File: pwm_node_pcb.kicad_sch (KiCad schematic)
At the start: 49 parts, among them J1 Battery, J2 5V Breakout, J3 TC2050-IDC-NL, J4 CAN1, J5 Load Source, U1 LMR51430, U2 LD1117S33CTR, U3 TJA1051T/3, U4 STM32L432KCU, U5 TXB0104QPWRQ1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

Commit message: Fix silkscreen and load caps to 220uF
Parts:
- C16, C17: value 2200u -> 220u
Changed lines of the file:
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@@
 	(title_block
 		(title "PWM Node")
-		(rev "v0.1.0-alpha")
+		(rev "v0.1.0")
 		(company "Daniel Jeon")
 	)
@@
 			)
 		)
-		(property "Value" "2200u"
+		(property "Value" "220u"
 			(at 117.348 185.42 0)
 			(effects
@@
 			)
 		)
-		(property "Value" "2200u"
+		(property "Value" "220u"
 			(at 104.648 185.42 0)
 			(effects

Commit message: Fix flipped UART breakout (TP) nets
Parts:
- TP1: value UART_RX -> UART_TX
- TP2: value UART_TX -> UART_RX
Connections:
- net USART1_RX: now also TP2.1, U4.30 (PB7); no longer TP1.1, U4.29 (PB6)
- net USART1_TX: now also TP1.1, U4.29 (PB6); no longer TP2.1, U4.30 (PB7)
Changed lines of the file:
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@@
 		)
 	)
-	(hierarchical_label "USART1_TX"
+	(hierarchical_label "USART1_RX"
 		(shape input)
-		(at 157.48 156.21 180)
+		(at 57.15 134.62 180)
 		(effects
 			(font
@@
 		)
 	)
-	(hierarchical_label "USART1_RX"
+	(hierarchical_label "USART1_TX"
 		(shape input)
-		(at 157.48 148.59 180)
+		(at 57.15 132.08 180)
 		(effects
 			(font
@@
 		)
 	)
-	(hierarchical_label "CAN1_TX"
+	(hierarchical_label "USART1_TX"
 		(shape input)
-		(at 217.17 81.28 180)
+		(at 157.48 148.59 180)
 		(effects
 			(font
@@
 		)
 	)
-	(hierarchical_label "USART1_TX"
+	(hierarchical_label "CAN1_TX"
 		(shape input)
-		(at 57.15 134.62 180)
+		(at 217.17 81.28 180)
 		(effects
 			(font
@@
 		)
 	)
-	(hierarchical_label "USART1_RX"
+	(hierarchical_label "CAN1_RX"
 		(shape input)
-		(at 57.15 132.08 180)
+		(at 82.55 129.54 0)
 		(effects
 			(font
 				(size 1.27 1.27)
 			)
-			(justify right)
+			(justify left)
 		)
 	)
-	(hierarchical_label "CAN1_RX"
+	(hierarchical_label "TIM1_CH4"
 		(shape input)
-		(at 82.55 129.54 0)
+		(at 241.3 143.51 0)
 		(effects
 			(font
@@
 		)
 	)
-	(hierarchical_label "TIM1_CH4"
+	(hierarchical_label "USART1_RX"
 		(shape input)
-		(at 241.3 143.51 0)
+		(at 157.48 156.21 180)
 		(effects
 			(font
 				(size 1.27 1.27)
 			)
-			(justify left)
+			(justify right)
 		)
 	)
@@
 			)
 		)
-		(property "Value" "UART_TX"
+		(property "Value" "UART_RX"
 			(at 163.83 157.4799 90)
 			(effects
@@
 			)
 		)
-		(property "Value" "UART_RX"
+		(property "Value" "UART_TX"
 			(at 163.83 149.8599 90)
 			(effects

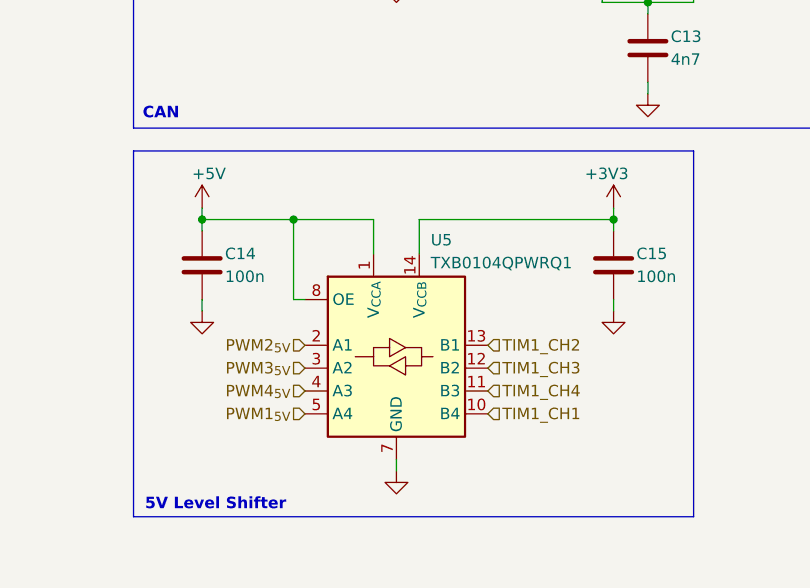
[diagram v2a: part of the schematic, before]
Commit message: Fix level shifter circuit
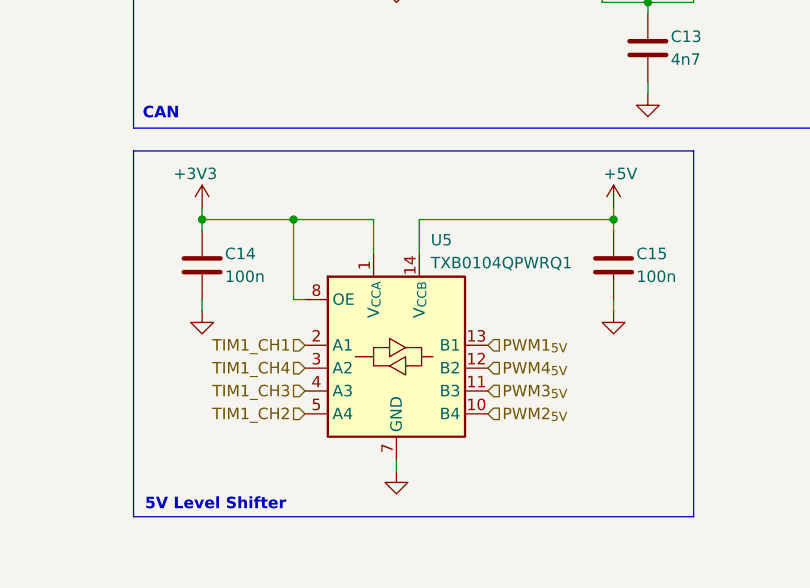
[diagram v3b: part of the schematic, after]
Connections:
- net +3V3: now also C14.1, U5.1 (V_{CCA}), U5.8 (OE); no longer C15.1, U5.14 (V_{CCB})
- net +5V: now also C15.1, U5.14 (V_{CCB}); no longer C14.1, U5.1 (V_{CCA}), U5.8 (OE)
- net PWM1_{5V}: now also U5.13 (B1); no longer U5.5 (A4)
- net PWM2_{5V}: now also U5.10 (B4); no longer U5.2 (A1)
- net PWM3_{5V}: now also U5.11 (B3); no longer U5.3 (A2)
- net PWM4_{5V}: now also U5.12 (B2); no longer U5.4 (A3)
- net TIM1_CH1: now also U5.2 (A1); no longer U5.10 (B4)
- net TIM1_CH2: now also U5.5 (A4); no longer U5.13 (B1)
- net TIM1_CH3: now also U5.4 (A3); no longer U5.12 (B2)
- net TIM1_CH4: now also U5.3 (A2); no longer U5.11 (B3)
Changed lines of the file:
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@@
 	)
 	(junction
+		(at 219.71 124.46)
+		(diameter 0)
+		(color 0 0 0 0)
+	)
+	(junction
 		(at 165.1 26.67)
 		(diameter 0)
@@
 	)
 	(junction
-		(at 219.71 124.46)
-		(diameter 0)
-		(color 0 0 0 0)
-	)
-	(junction
 		(at 209.55 124.46)
 		(diameter 0)
@@
 	(wire
 		(pts
+			(xy 219.71 124.46) (xy 228.6 124.46)
+		)
+		(stroke
+			(width 0)
+			(type default)
+		)
+	)
+	(wire
+		(pts
 			(xy 54.61 31.75) (xy 55.88 31.75)
 		)
@@
 	(wire
 		(pts
-			(xy 219.71 124.46) (xy 228.6 124.46)
-		)
-		(stroke
-			(width 0)
-			(type default)
-		)
-	)
-	(wire
-		(pts
 			(xy 76.2 80.01) (xy 76.2 81.28)
 		)
@@
 		)
 	)
-	(hierarchical_label "TIM1_CH1"
+	(hierarchical_label "PWM4_{5V}"
 		(shape input)
-		(at 241.3 146.05 0)
+		(at 241.3 140.97 0)
 		(effects
 			(font
@@
 	(hierarchical_label "PWM3_{5V}"
 		(shape input)
-		(at 220.98 140.97 180)
+		(at 241.3 143.51 0)
 		(effects
 			(font
 				(size 1.27 1.27)
 			)
-			(justify right)
+			(justify left)
 		)
 	)
@@
 		)
 	)
-	(hierarchical_label "TIM1_CH2"
+	(hierarchical_label "SWO"
 		(shape input)
-		(at 241.3 138.43 0)
+		(at 36.83 38.1 0)
 		(effects
 			(font
@@
 		)
 	)
-	(hierarchical_label "SWO"
+	(hierarchical_label "PWM2_{5V}"
 		(shape input)
-		(at 36.83 38.1 0)
+		(at 241.3 146.05 0)
 		(effects
 			(font
@@
 		)
 	)
-	(hierarchical_label "PWM2_{5V}"
-		(shape input)
-		(at 220.98 138.43 180)
-		(effects
-			(font
-				(size 1.27 1.27)
-			)
-			(justify right)
-		)
-	)
 	(hierarchical_label "PWM1_{5V}"
 		(shape input)
@@
 		)
 	)
-	(hierarchical_label "PWM1_{5V}"
+	(hierarchical_label "TIM1_CH4"
 		(shape input)
-		(at 220.98 146.05 180)
+		(at 220.98 140.97 180)
 		(effects
 			(font
@@
 		)
 	)
-	(hierarchical_label "CAN1_TX"
+	(hierarchical_label "TIM1_CH1"
 		(shape input)
-		(at 82.55 132.08 0)
+		(at 220.98 138.43 180)
 		(effects
 			(font
 				(size 1.27 1.27)
 			)
-			(justify left)
+			(justify right)
 		)
 	)
-	(hierarchical_label "CAN1_RX"
+	(hierarchical_label "CAN1_TX"
 		(shape input)
-		(at 217.17 83.82 180)
+		(at 82.55 132.08 0)
 		(effects
 			(font
 				(size 1.27 1.27)
 			)
-			(justify right)
+			(justify left)
 		)
 	)
-	(hierarchical_label "PWM4_{5V}"
+	(hierarchical_label "CAN1_RX"
 		(shape input)
-		(at 220.98 143.51 180)
+		(at 217.17 83.82 180)
 		(effects
 			(font
@@
 		)
 	)
-	(hierarchical_label "USART1_TX"
+	(hierarchical_label "TIM1_CH3"
 		(shape input)
-		(at 157.48 148.59 180)
+		(at 220.98 143.51 180)
 		(effects
 			(font
@@
 		)
 	)
-	(hierarchical_label "CAN1_TX"
+	(hierarchical_label "TIM1_CH2"
 		(shape input)
-		(at 217.17 81.28 180)
+		(at 220.98 146.05 180)
 		(effects
 			(font
@@
 		)
 	)
-	(hierarchical_label "SWDIO"
+	(hierarchical_label "USART1_TX"
 		(shape input)
-		(at 36.83 35.56 0)
+		(at 157.48 148.59 180)
 		(effects
 			(font
 				(size 1.27 1.27)
 			)
-			(justify left)
+			(justify right)
 		)
 	)
-	(hierarchical_label "TIM1_CH3"
+	(hierarchical_label "CAN1_TX"
 		(shape input)
-		(at 241.3 140.97 0)
+		(at 217.17 81.28 180)
+		(effects
+			(font
+				(size 1.27 1.27)
+			)
+			(justify right)
+		)
+	)
+	(hierarchical_label "SWDIO"
+		(shape input)
+		(at 36.83 35.56 0)
 		(effects
 			(font
@@
 		)
 	)
-	(hierarchical_label "TIM1_CH4"
+	(hierarchical_label "PWM1_{5V}"
 		(shape input)
-		(at 241.3 143.51 0)
+		(at 241.3 138.43 0)
 		(effects
 			(font
@@
 	(symbol
 		(lib_id "power:+3V3")
-		(at 255.27 123.19 0)
+		(at 209.55 123.19 0)
 		(unit 1)
 		(exclude_from_sim no)
@@
 		(dnp no)
 		(property "Reference" "#PWR033"
-			(at 255.27 127 0)
+			(at 209.55 127 0)
 			(effects
 				(font
@@
 		)
 		(property "Value" "+3V3"
-			(at 254.508 119.38 0)
+			(at 208.788 119.38 0)
 			(effects
 				(font
@@
 		)
 		(property "Footprint" ""
-			(at 255.27 123.19 0)
+			(at 209.55 123.19 0)
 			(effects
 				(font
@@
 		)
 		(property "Datasheet" ""
-			(at 255.27 123.19 0)
+			(at 209.55 123.19 0)
 			(effects
 				(font
@@
 		)
 		(property "Description" "Power symbol creates a global label with name \"+3V3\""
-			(at 255.27 123.19 0)
+			(at 209.55 123.19 0)
 			(effects
 				(font
@@
 	(symbol
 		(lib_id "power:+5V")
-		(at 209.55 123.19 0)
+		(at 255.27 123.19 0)
 		(unit 1)
 		(exclude_from_sim no)
@@
 		(dnp no)
 		(property "Reference" "#PWR032"
-			(at 209.55 127 0)
+			(at 255.27 127 0)
 			(effects
 				(font
@@
 		)
 		(property "Value" "+5V"
-			(at 210.312 119.38 0)
+			(at 256.032 119.38 0)
 			(effects
 				(font
@@
 		)
 		(property "Footprint" ""
-			(at 209.55 123.19 0)
+			(at 255.27 123.19 0)
 			(effects
 				(font
@@
 		)
 		(property "Datasheet" ""
-			(at 209.55 123.19 0)
+			(at 255.27 123.19 0)
 			(effects
 				(font
@@
 		)
 		(property "Description" "Power symbol creates a global label with name \"+5V\""
-			(at 209.55 123.19 0)
+			(at 255.27 123.19 0)
 			(effects
 				(font

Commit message: Update sch and pcb sheet info
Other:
- title: PWM Node -> PWM Node PCB
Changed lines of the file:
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@@
 	(paper "A4")
 	(title_block
-		(title "PWM Node")
-		(rev "v0.1.0")
+		(title "PWM Node PCB")
+		(rev "0.1.0")
 		(company "Daniel Jeon")
 	)

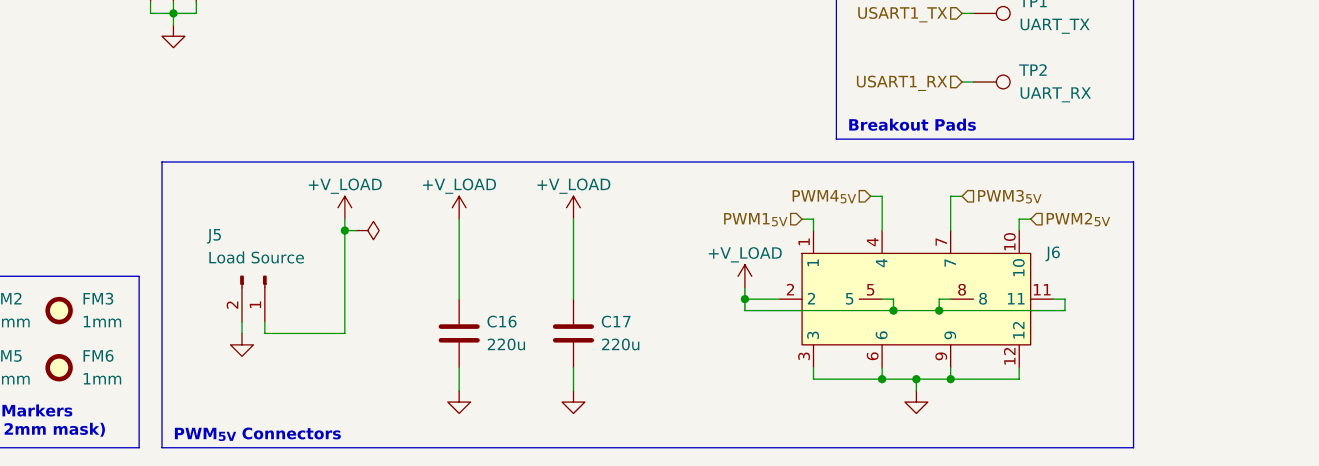
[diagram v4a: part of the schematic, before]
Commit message: Fix load cap fp and remove dedicated supply
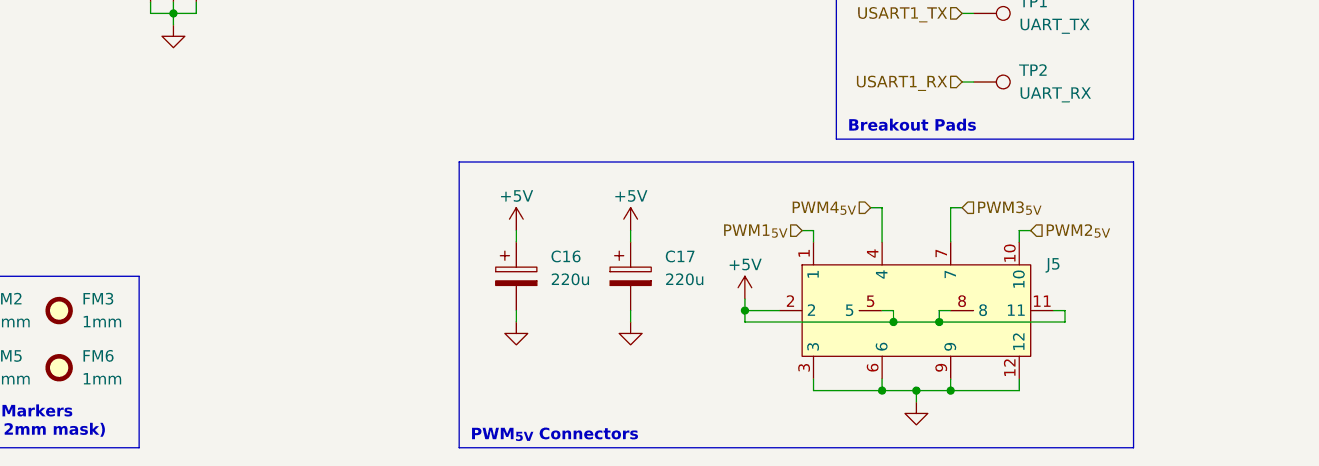
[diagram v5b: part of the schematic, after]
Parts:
- removed C16, C17: 220u, Capacitor_SMD:C_Elec_3x5.4, symbol Device:C
- removed J5: Load Source, pwm_node_connectors:battery, symbol Connector:Conn_01x02_Pin
- added C16, C17: 220u, Capacitor_SMD:CP_Elec_6.3x5.2, symbol Device:C_Polarized
- renumbered J6 to J5
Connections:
- net +V_LOAD is gone; now on net +5V: J5.11, J5.2, J5.5, J5.8
- net +5V: now also C16.1, C17.1
- net GND: now also C16.2, C17.2
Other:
- moved on the sheet: J5

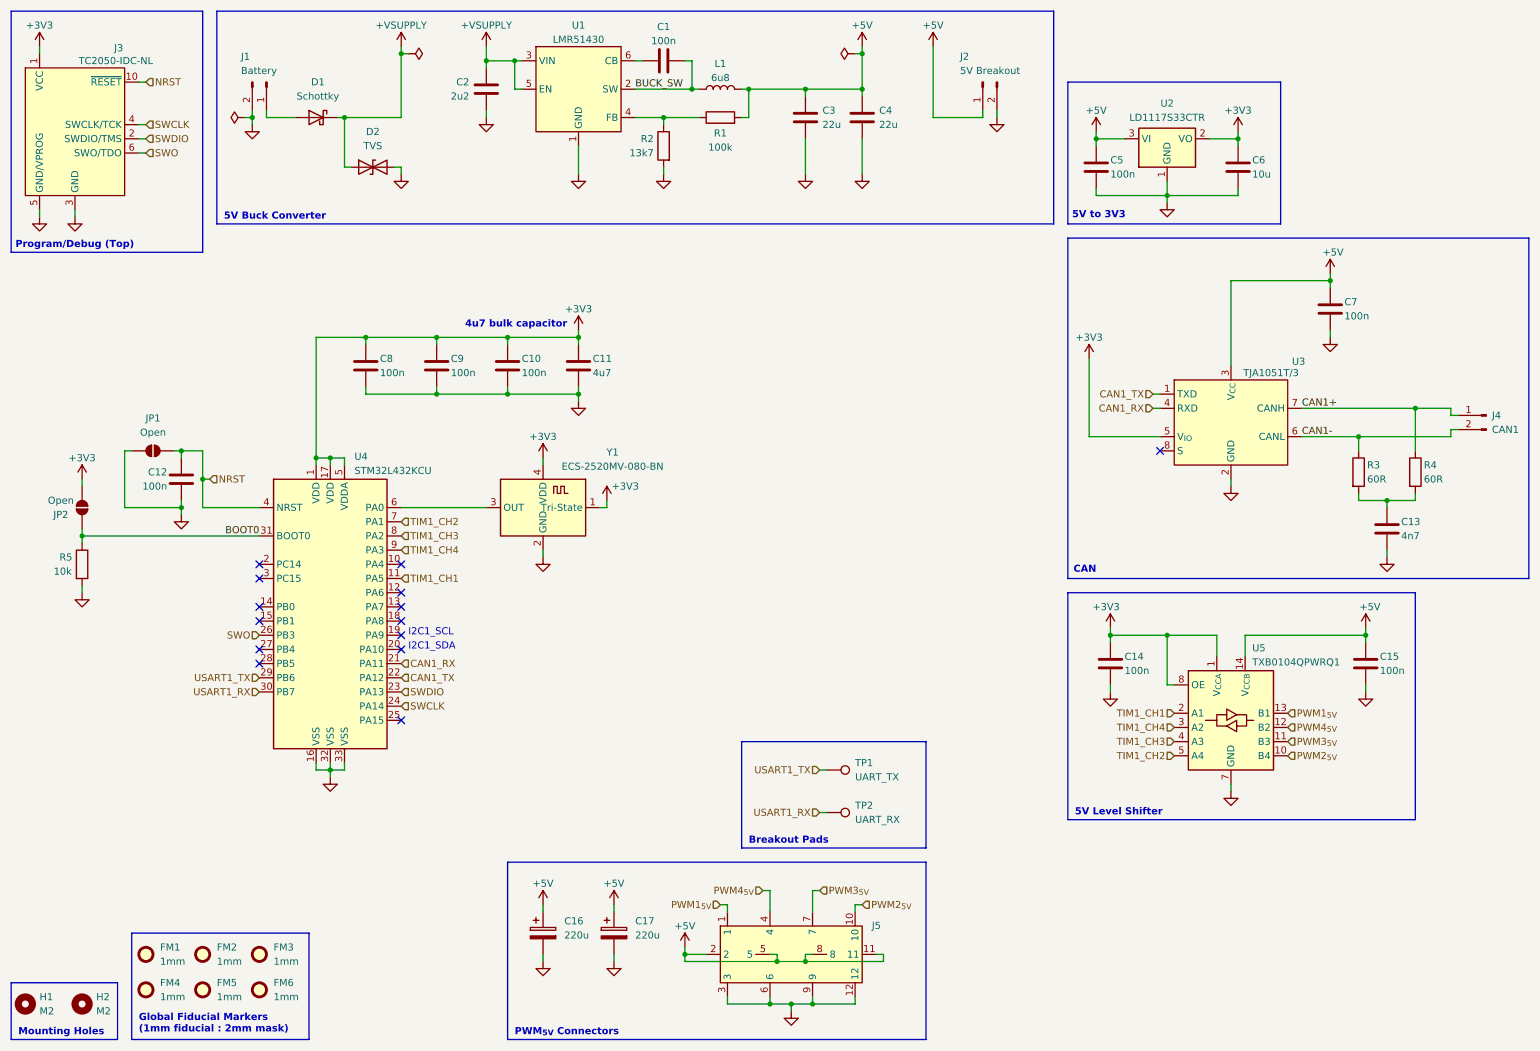
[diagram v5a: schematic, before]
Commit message: Add TVS and schottky diode info
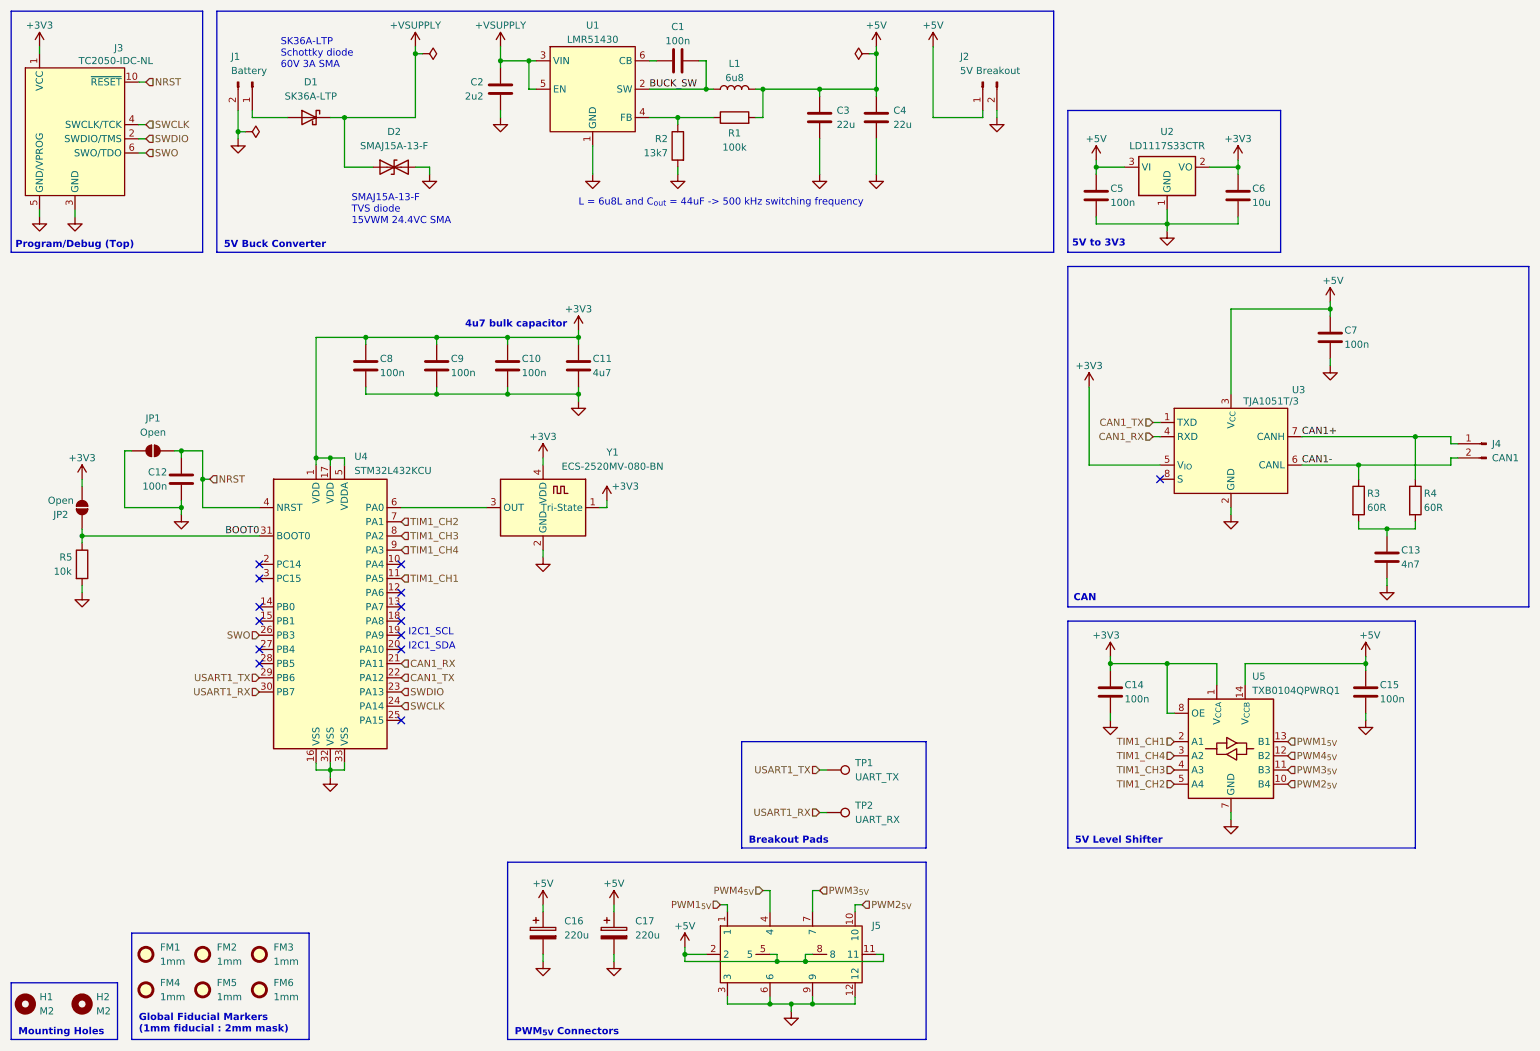
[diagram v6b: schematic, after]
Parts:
- D1: value Schottky -> SK36A-LTP
- D2: value TVS -> SMAJ15A-13-F
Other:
- note added: "L = 6u8L and C_{out} = 44uF -> 500 kHz switching frequency"
- note added: "SK36A-LTP Schottky diode 60V 3A SMA"
- note added: "SMAJ15A-13-F TVS diode 15VWM 24.4VC SMA"
- moved on the sheet: C13, C14, C15, C5, C6, C7, J4, R3, R4, U2, U3, U5
